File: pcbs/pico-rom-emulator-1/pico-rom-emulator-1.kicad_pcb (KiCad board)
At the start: 2 copper layers, 19 parts, among them J1 Conn_01x03_Female, J2 Conn_01x03_Female, U1 74LS245, U2 74LS245, U3 27C512, U4 74LS245, U5 74LS245, U6 Pico

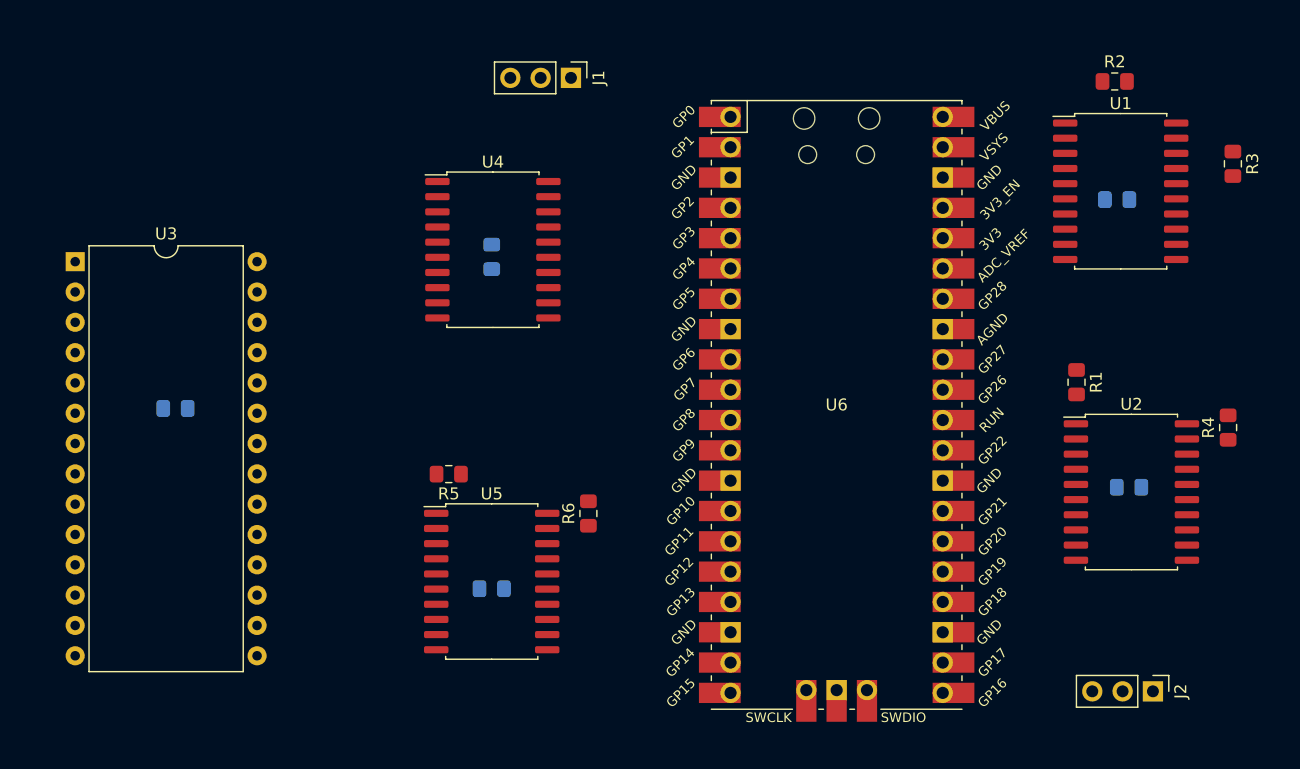
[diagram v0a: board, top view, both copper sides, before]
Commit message: Added C code for emulator
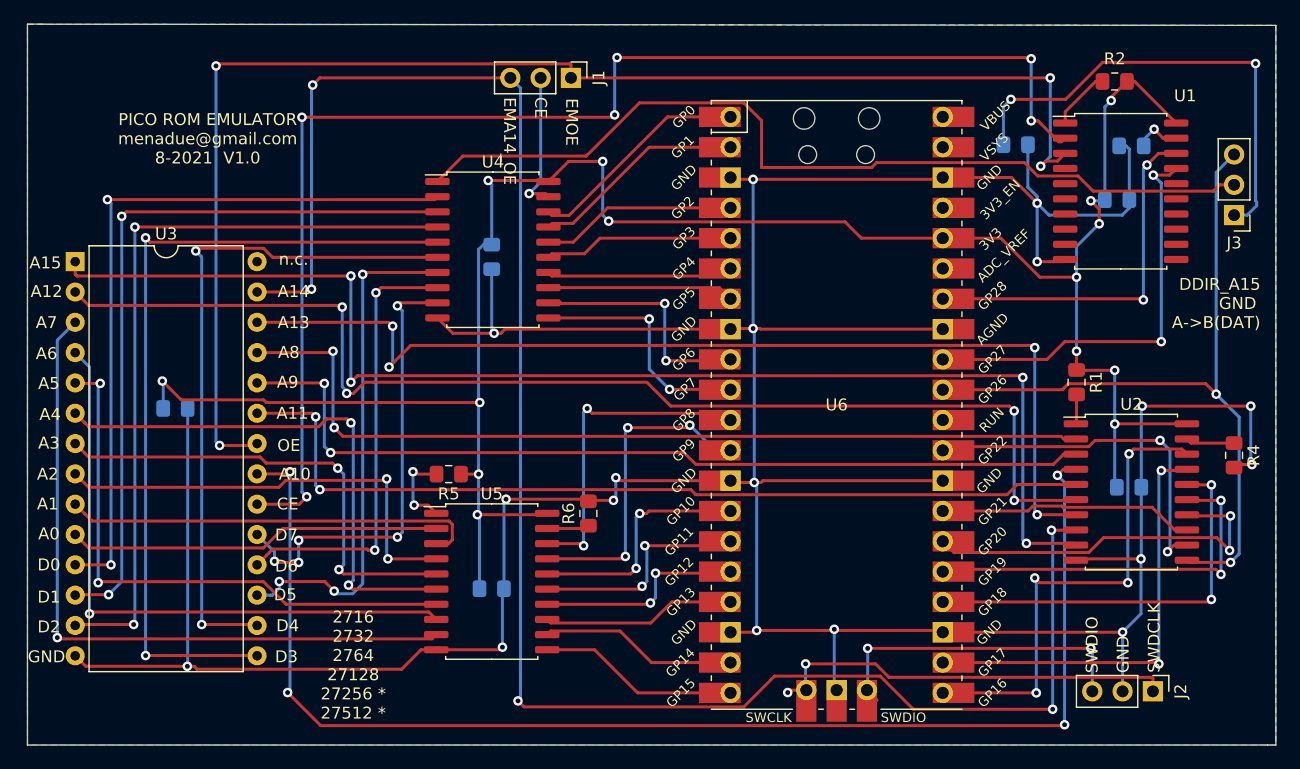
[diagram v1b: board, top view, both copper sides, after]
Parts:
- added J3: Conn_01x03_Female, Connector_PinHeader_2.54mm:PinHeader_1x03_P2.54mm_Vertical, F.Cu at (256.7, 81.7)
- added R7: R_Small, Resistor_SMD:R_0805_2012Metric_Pad1.15x1.40mm_HandSolder, B.Cu at (238.4, 75.8)
- R3: moved to B.Cu
- moved R3 8.63 mm to (248.1, 75.9), turned to 180 degrees
- moved R4 2.38 mm to (256.7, 101.8), turned to 270 degrees
- turned R2 to 180 degrees
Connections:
- J1 pad 3: A14_OE -> EMA14_OE
- J2 pad 1: Net-(J2-Pad1) -> SWCLK
- J2 pad 3: Net-(J2-Pad3) -> SWDIO
- U2 pad 11: A15 -> DDIR_A15
- U2 pad 8: (no net) -> EMA14_OE
- U2 pad 9: (no net) -> EMA15
- U3 pad 1: A15 -> EMA15
- U3 pad 27: A14_OE -> EMA14_OE
- U4 pad 1: (no net) -> Net-(J3-Pad2)
- U6 pad 31: A15 -> DDIR_A15
- U6 pad 41: Net-(J2-Pad3) -> SWCLK
- U6 pad 43: Net-(J2-Pad1) -> SWDIO
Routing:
- net GND: track 0.00 -> 333.8 mm, vias 0 -> 18
- net +3V3: track 0.00 -> 180.9 mm, vias 0 -> 14
- net EMA14_OE: track 0.00 -> 155.6 mm, vias 0 -> 5
- net EMOE: track 0.00 -> 116.5 mm, vias 0 -> 4
- net EMCE: track 0.00 -> 111.2 mm, vias 0 -> 6
- net EMA10: track 0.00 -> 110.6 mm, vias 0 -> 4
- net EMA15: track 0.00 -> 107.9 mm, vias 0 -> 4
- net EMA12: track 0.00 -> 100.3 mm, vias 0 -> 4
- net EMA13: track 0.00 -> 87.3 mm, vias 0 -> 4
- net Net-(J3-Pad2): track 0.00 -> 75.4 mm
- net EMA8: track 0.00 -> 75.4 mm, vias 0 -> 2
- net EMA11: track 0.00 -> 75.2 mm, vias 0 -> 2
- net EMA9: track 0.00 -> 74.9 mm, vias 0 -> 2
- net EMD3: track 0.00 -> 68.9 mm, vias 0 -> 2
- net EMD2: track 0.00 -> 63.6 mm, vias 0 -> 2
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- added copper zone on B.Cu, net GND
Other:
- board outline added: 104.6 x 60.4 mm
- board text added: "2716 2732 2764 27128 27256 * 27512 *"
- board text added: "A->B(DAT)"
- board text added: "A0"
- board text added: "A1"
- board text added: "A10"
- board text added: "A11"
- board text added: "A12"
- board text added: "A13"
- board text added: "A14"
- board text added: "A15"
- board text added: "A2"
- board text added: "A3"
- board text added: "A4"
- board text added: "A5"
- board text added: "A6"
- board text added: "A7"
- board text added: "A8"
- board text added: "A9"
- board text added: "CE"
- board text added: "D0"
- board text added: "D1"
- board text added: "D2"
- board text added: "D3"
- board text added: "D4"
- board text added: "D5"
- board text added: "D6"
- board text added: "D7"
- board text added: "DDIR_A15"
- board text added: "EMA14_OE"
- board text added: "EMOE"
- board text added: "GND"
- board text added: "OE"
- board text added: "PICO ROM EMULATOR menadue@gmail.com 8-2021 V1.0"
- board text added: "SWDCLK"
- board text added: "SWDIO"
- board text added: "n.c."
